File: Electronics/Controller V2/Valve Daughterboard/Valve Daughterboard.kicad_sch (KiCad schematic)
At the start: 25 parts, among them J1 Conn_01x08, J10 Conn_01x10, J11 Conn_01x02, J12 Conn_01x02, J13 Conn_01x02, J14 Conn_01x02, J15 Conn_01x02, J16 Conn_01x02, J17 Conn_01x02, J18 Conn_01x02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

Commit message: Completed daughterboards.
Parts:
- H1, H2, H3, H4: footprint MountingHole:MountingHole_3.2mm_M3 -> MountingHole:MountingHole_6.4mm_M6
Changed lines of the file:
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@@
       (effects (font (size 1.27 1.27)) (justify left))
     )
-    (property "Footprint" "MountingHole:MountingHole_3.2mm_M3" (at 91.44 151.765 0)
+    (property "Footprint" "MountingHole:MountingHole_6.4mm_M6" (at 91.44 151.765 0)
       (effects (font (size 1.27 1.27)) hide)
     )
@@
       (effects (font (size 1.27 1.27)) (justify left))
     )
-    (property "Footprint" "MountingHole:MountingHole_3.2mm_M3" (at 91.44 158.115 0)
+    (property "Footprint" "MountingHole:MountingHole_6.4mm_M6" (at 91.44 158.115 0)
       (effects (font (size 1.27 1.27)) hide)
     )
@@
       (effects (font (size 1.27 1.27)) (justify left))
     )
-    (property "Footprint" "MountingHole:MountingHole_3.2mm_M3" (at 111.125 151.765 0)
+    (property "Footprint" "MountingHole:MountingHole_6.4mm_M6" (at 111.125 151.765 0)
       (effects (font (size 1.27 1.27)) hide)
     )
@@
       (effects (font (size 1.27 1.27)) (justify left))
     )
-    (property "Footprint" "MountingHole:MountingHole_3.2mm_M3" (at 111.125 158.115 0)
-      (effects (font (size 1.27 1.27)) hide)
-    )
+    (property "Footprint" "MountingHole:MountingHole_6.4mm_M6" (at 111.125 158.115 0)
+      (effects (font (size 1.27 1.27)) hide)
+    )

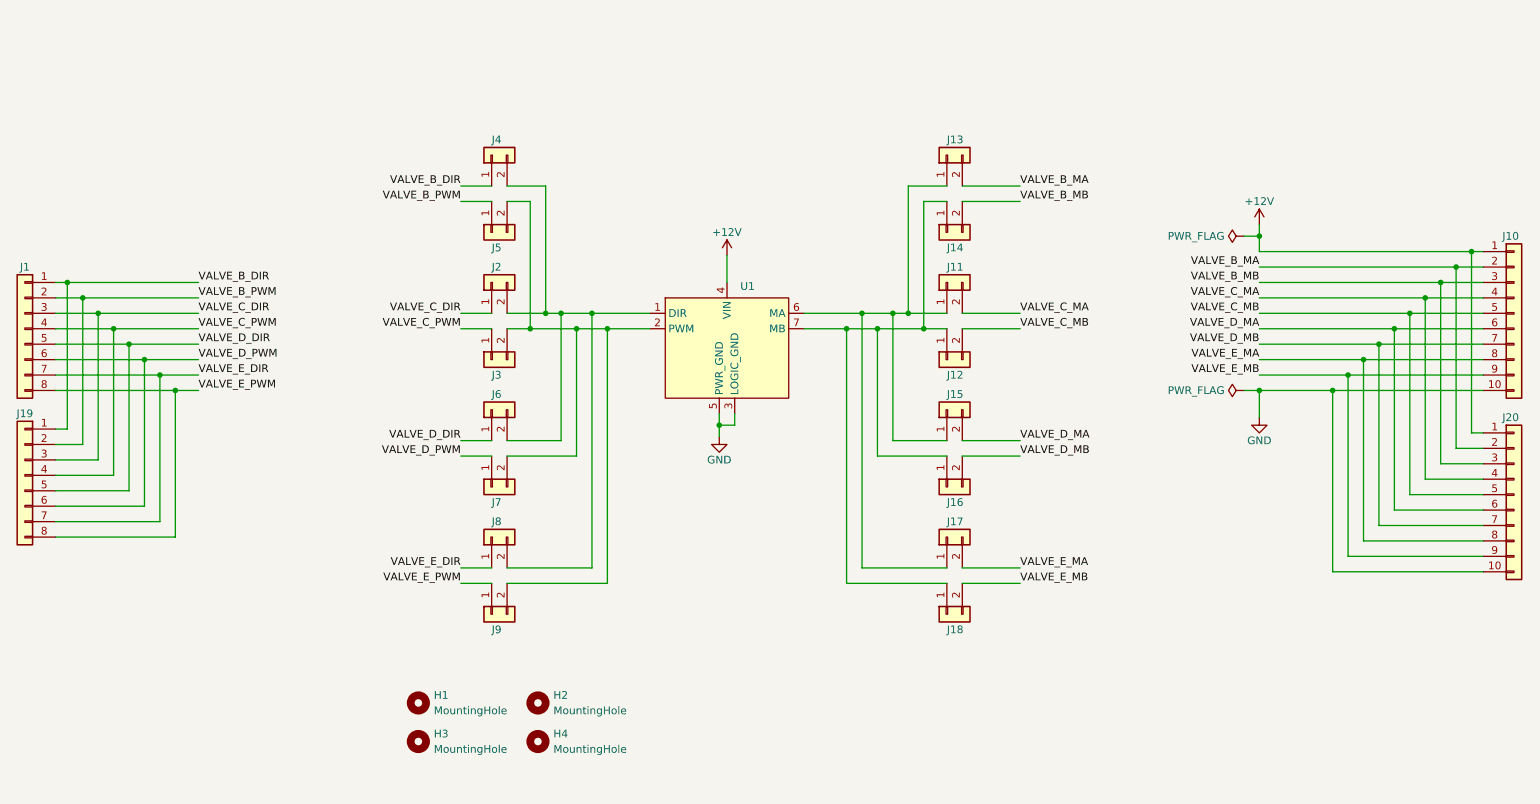
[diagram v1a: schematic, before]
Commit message: Added relay to control output of valve E.
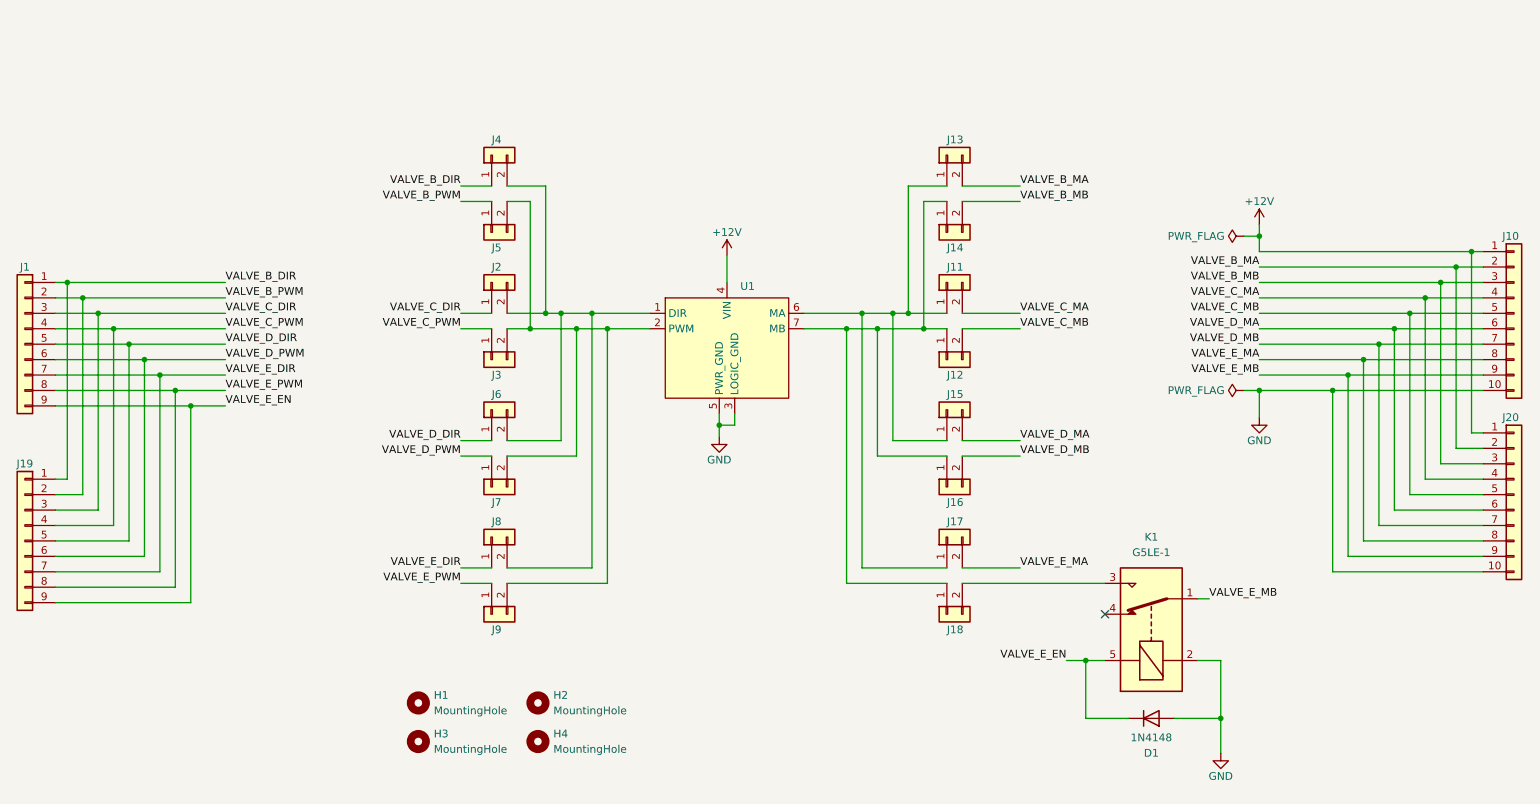
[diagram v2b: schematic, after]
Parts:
- added D1: 1N4148, Diode_THT:D_DO-35_SOD27_P7.62mm_Horizontal, symbol Diode:1N4148
- added K1: G5LE-1, Relay_THT:Relay_SPDT_Omron-G5LE-1, symbol Relay:G5LE-1
- J1, J19: footprint Connector_JST:JST_PH_B8B-PH-K_1x08_P2.00mm_Vertical -> Connector_JST:JST_PH_B9B-PH-K_1x09_P2.00mm_Vertical; symbol Connector_Generic:Conn_01x08 -> Connector_Generic:Conn_01x09
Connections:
- net GND: now also D1.2 (A), K1.2
- net VALVE_E_MB: now also K1.1; no longer J18.2 (Pin_2)
- new net: J18.2 (Pin_2), K1.3
- new net VALVE_E_EN: D1.1 (K), J1.9 (Pin_9), J19.9 (Pin_9), K1.5
- no-connect marks 0 -> 1

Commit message: Working on autosteer support for V2 controller.
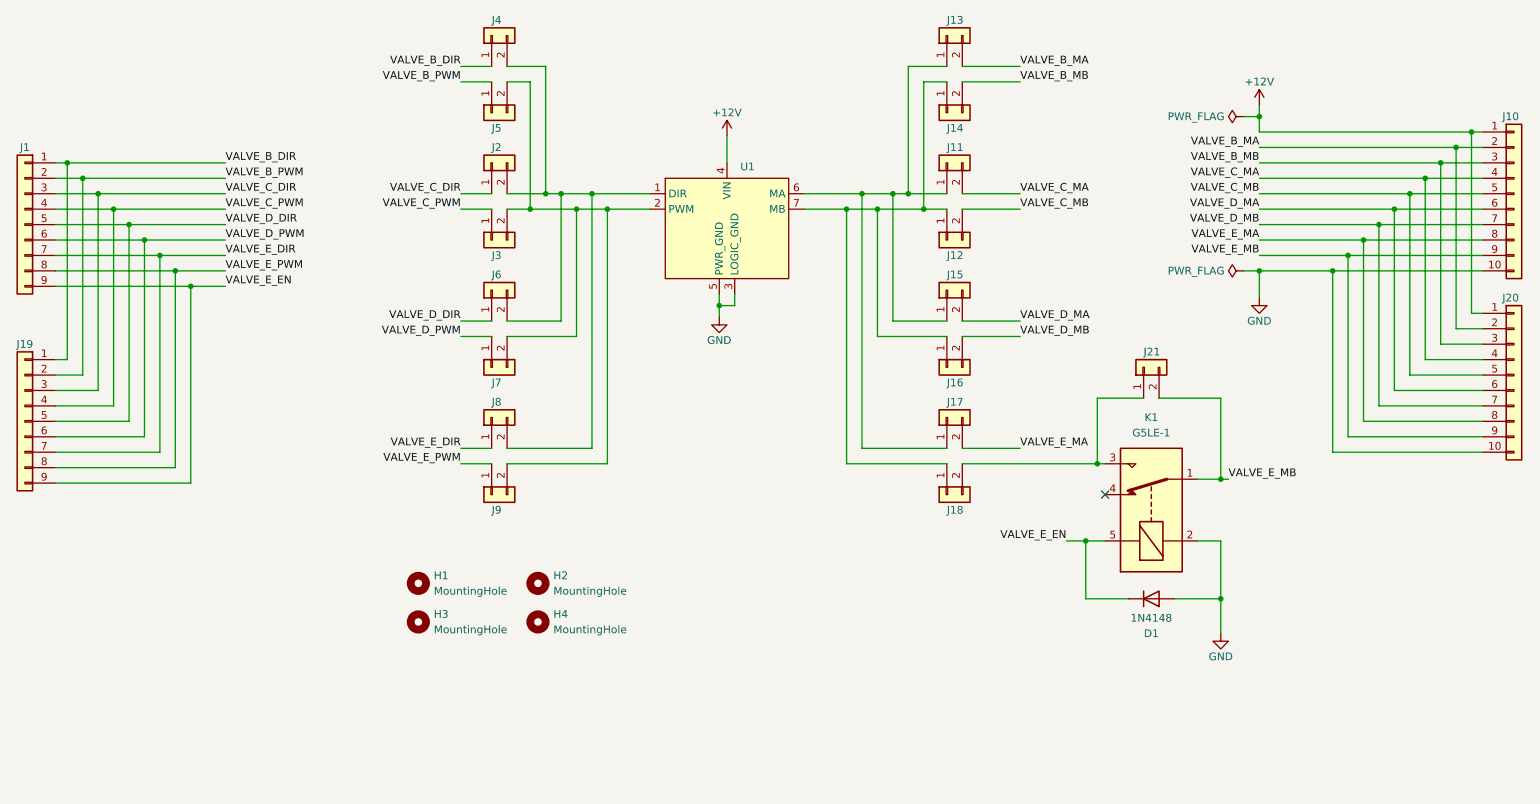
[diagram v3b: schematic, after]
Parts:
- added J21: Conn_01x02, Connector_PinHeader_2.54mm:PinHeader_1x02_P2.54mm_Vertical, symbol Connector_Generic:Conn_01x02
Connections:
- net VALVE_E_MB: now also J21.2 (Pin_2)
- net at J18.2 (Pin_2), K1.3: now also J21.1 (Pin_1)
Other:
- moved on the sheet: D1, H1, H2, H3, H4, J1, J10, J11, J12, J13, J14, J15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

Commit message: Added connector to valve daugherboard for optional 12V to 24V converter.
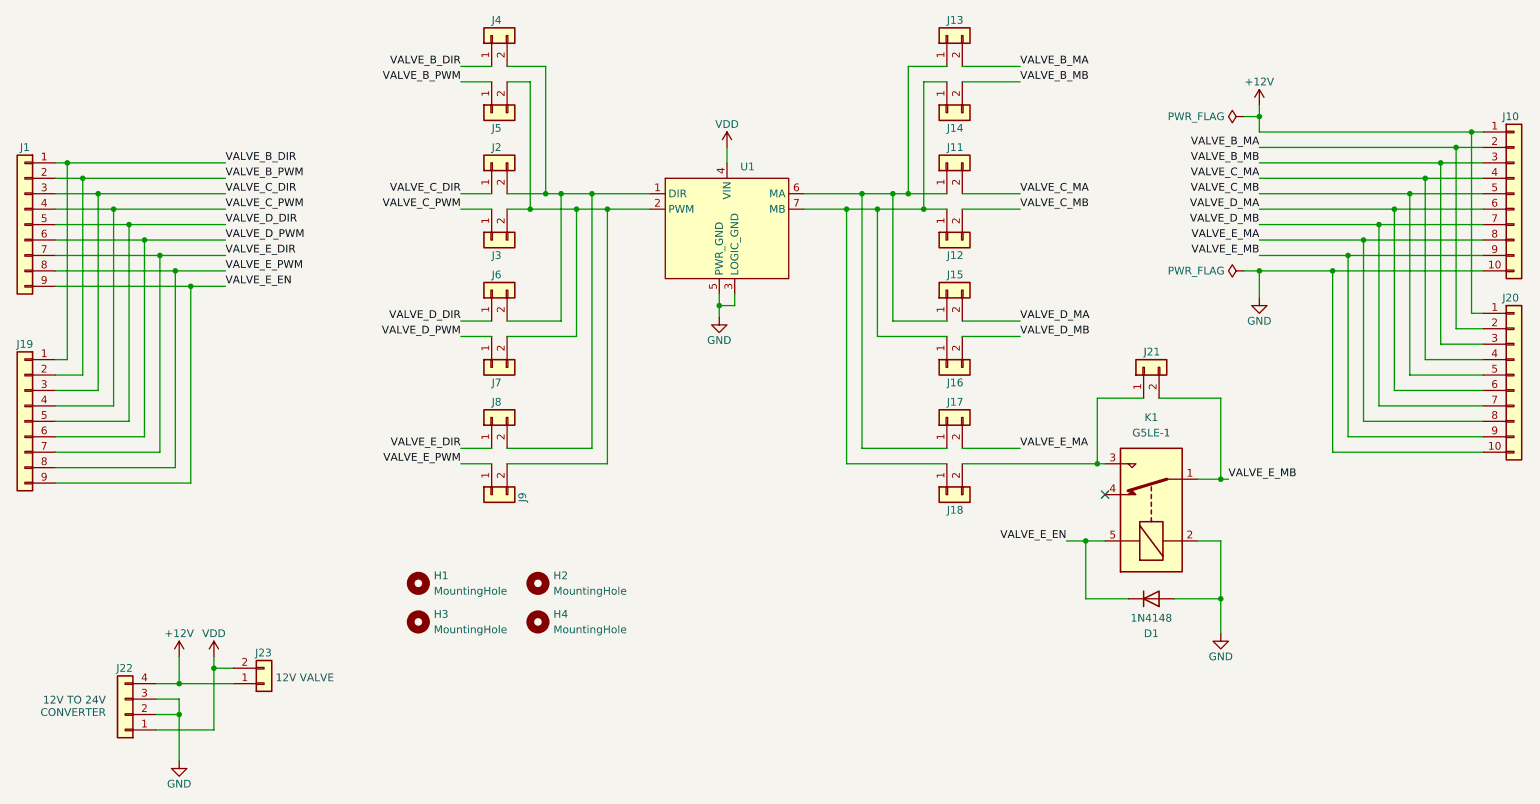
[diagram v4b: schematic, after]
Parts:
- added J22: Conn_01x04, Connector_JST:JST_XH_B4B-XH-A_1x04_P2.50mm_Vertical, symbol Connector_Generic:Conn_01x04
- added J23: Conn_01x02, Connector_PinHeader_2.54mm:PinHeader_1x02_P2.54mm_Vertical, symbol Connector_Generic:Conn_01x02
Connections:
- net +12V: now also J22.4 (Pin_4), J23.1 (Pin_1); no longer U1.4 (VIN)
- net GND: now also J22.2 (Pin_2), J22.3 (Pin_3)
- new net VDD: J22.1 (Pin_1), J23.2 (Pin_2), U1.4 (VIN)
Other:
- note added: "12V TO 24V CONVERTER"
- note added: "12V VALVE"
